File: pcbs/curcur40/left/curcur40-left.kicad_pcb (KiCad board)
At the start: 2 copper layers, 124.3 x 91.8 mm, 79 parts, among them J1 TYPE-C-31-M-13C, J2 TRS, J4 Conn_01x03, SW1 SW_Push, SW10 SW_Push, SW11 SW_Push, SW12 SW_Push, SW13 SW_Push, SW14 SW_Push, SW15 SW_Push, SW16 SW_Push, SW17 SW_Push, SW18 SW_Push, SW2 SW_Push, SW3 SW_Push, SW4 SW_Push, SW5 SW_Push, SW6 SW_Push, SW7 SW_Push, SW8 SW_Push, SW9 SW_Push, U1 RP2040, U2 NCP1117LPST33T3G, U3 TPD4E05U06DQAR, U4 W25Q128JVSIQ, Y1 12MHz 18pF

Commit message: fix
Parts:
- U4: footprint Package_SO:SOIC-8_5.23x5.23mm_P1.27mm -> Package_SO:SOIC-8_5.3x5.3mm_P1.27mm
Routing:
- net Net-(D1-K): track 558.8 -> 552.0 mm, vias 34 -> 32
- net +5V: track 134.4 -> 129.8 mm
- net GND: track 208.4 -> 206.3 mm
- net Net-(EXLED1-DIN): track 135.9 -> 135.1 mm, vias 5 -> 4
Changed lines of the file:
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@@
 		)
 	)
-	(footprint "Package_SO:SOIC-8_5.23x5.23mm_P1.27mm"
+	(footprint "Package_SO:SOIC-8_5.3x5.3mm_P1.27mm"
 		(layer "B.Cu")
 		(at -62.4925 34.64)
@@
 	)
 	(segment
-		(start -29.11475 25.96025)
-		(end -30.5375 24.5375)
-		(width 0.508)
-		(layer "B.Cu")
-		(net "GND")
-	)
-	(segment
 		(start -30.2375 48.65)
 		(end -30.2375 58.2875)
@@
 	)
 	(segment
-		(start -6.5425 38.62)
+		(start -8.5 38.62)
 		(end -24.762 38.62)
 		(width 0.4)
@@
 	)
 	(segment
-		(start -39.235992 41.23995)
-		(end -39.9125 41.23995)
-		(width 0.2032)
-		(layer "F.Cu")
-		(net "+5V")
-	)
-	(segment
 		(start -39.240942 41.235)
 		(end -46.24245 41.235)
@@
 	(segment
 		(start -24.832 30.596)
-		(end -6.5425 30.596)
+		(end -8.5 30.596)
 		(width 0.4)
 		(layer "F.Cu")
@@
 	(segment
 		(start -8.5 38.62)
-		(end -6.5425 38.62)
+		(end -6.5425 38.54625)
 		(width 0.4)
 		(layer "B.Cu")
@@
 	(segment
 		(start -8.5 30.596)
-		(end -6.5425 30.596)
+		(end -6.5425 30.74625)
 		(width 0.4)
 		(layer "B.Cu")
@@
 	)
 	(segment
-		(start -114.5425 4.968751)
-		(end -112.852498 4.968751)
-		(width 0.508)
-		(layer "F.Cu")
-		(net "Net-(D1-K)")
-	)
-	(segment
 		(start -74.2375 -1.663748)
 		(end -73.732498 -2.16875)
@@
 	)
 	(segment
-		(start -112.8325 23.79125)
-		(end -114.9725 23.79125)
-		(width 0.508)
-		(layer "F.Cu")
-		(net "Net-(D1-K)")
-	)
-	(segment
 		(start -112.3275 -13.38505)
 		(end -112.3275 -13.63375)
@@
 	)
 	(segment
-		(start -117.8625 -14.36875)
-		(end -116.4114 -14.36875)
-		(width 0.508)
-		(layer "F.Cu")
-		(net "Net-(D1-K)")
-	)
-	(segment
 		(start -50.15 46.462)
 		(end -50.65 45.4)
@@
 	)
 	(via
-		(at -114.5425 4.968751)
-		(size 0.6)
-		(drill 0.4)
-		(layers "F.Cu" "B.Cu")
-		(capping no)
-		(covering
-			(front no)
-			(back no)
-		)
-		(plugging
-			(front no)
-			(back no)
-		)
-		(filling no)
-		(net "Net-(D1-K)")
-	)
-	(via
 		(at -74.70125 18.375)
 		(size 0.6)
@@
 	)
 	(via
-		(at -114.9725 23.79125)
-		(size 0.6)
-		(drill 0.4)
-		(layers "F.Cu" "B.Cu")
-		(capping no)
-		(covering
-			(front no)
-			(back no)
-		)
-		(plugging
-			(front no)
-			(back no)
-		)
-		(filling no)
-		(net "Net-(D1-K)")
-	)
-	(via
 		(at -23.5 40.135)
 		(size 0.5)
@@
 	)
 	(segment
-		(start -115.6225 24.44125)
-		(end -114.9725 23.79125)
-		(width 0.508)
-		(layer "B.Cu")
-		(net "Net-(D1-K)")
-	)
-	(segment
 		(start -17.08 13.6125)
 		(end -17.0725 13.605)
@@
 	)
 	(segment
-		(start -114.5425 4.968751)
-		(end -115.014999 5.44125)
-		(width 0.508)
-		(layer "B.Cu")
-		(net "Net-(D1-K)")
-	)
-	(segment
 		(start -25.402502 -4.5825)
 		(end -26.4625 -5.642498)
@@
 	)
 	(segment
-		(start -112.9191 -11.76285)
-		(end -112.3375 -11.18125)
-		(width 0.2032)
-		(layer "F.Cu")
-		(net "Net-(EXLED1-DIN)")
-	)
-	(segment
 		(start -20.0225 -4.6915)
 		(end -18.04025 -4.6915)
@@
 		(size 0.6)
 		(drill 0.4)
-		(layers "F.Cu" "B.Cu")
-		(capping no)
-		(covering
-			(front no)
-			(back no)
-		)
-		(plugging
-			(front no)
-			(back no)
-		)
-		(filling no)
-		(net "Net-(EXLED1-DIN)")
-	)
-	(via
-		(at -112.3375 -11.18125)
-		(size 0.6)
-		(drill 0.4)

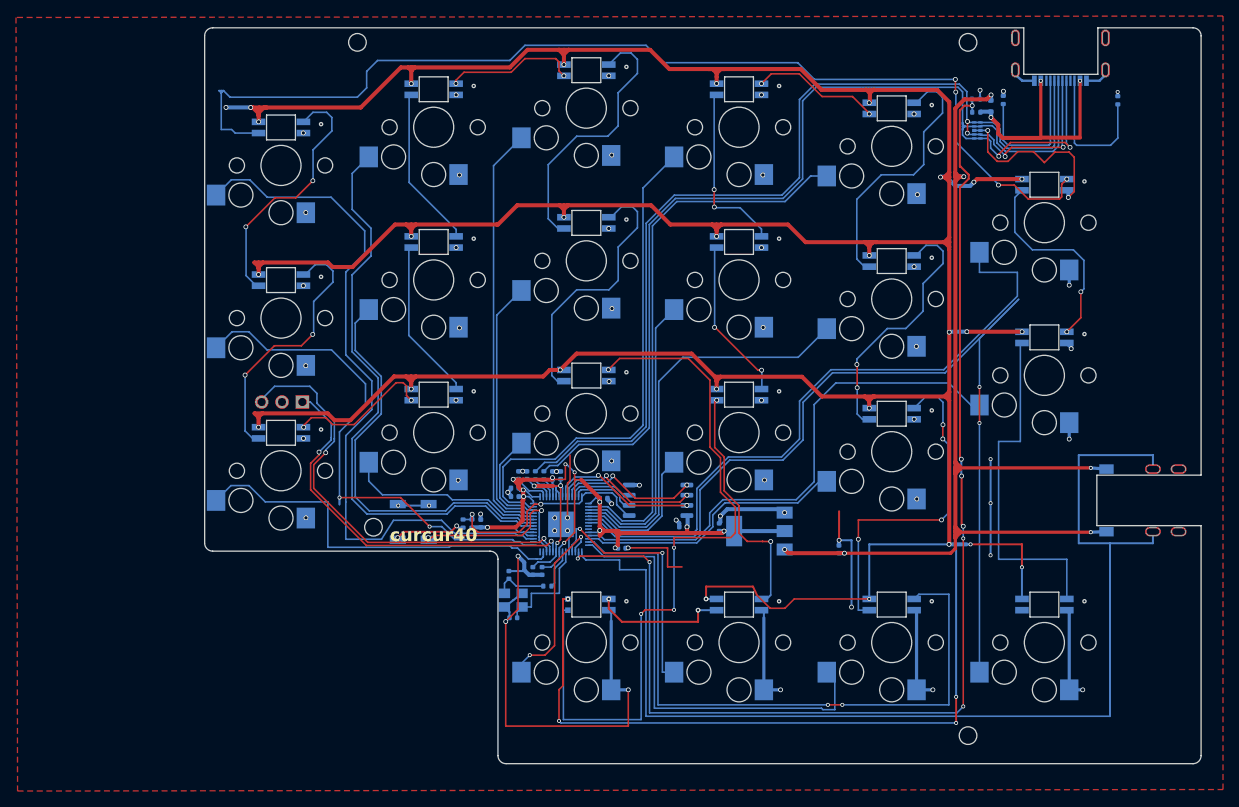
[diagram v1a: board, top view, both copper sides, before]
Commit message: 🔴 1. 致命的な不具合（Critical：物理的に組立不可、または動作不可）
[Critical-1] トラックボール部の3D機構・光学設計の破綻（4重の物理的干渉・焦点外れ）
[Critical-2] 左右メイン基板の取付穴径が ∅2.20 mm になっており、M2スペーサーが貫通できない
[Critical-3] 3Dプリントケース内部の 2.0mm スペーサー受けボスが消失しており、高さが 2.0 mm 合わない
[Critical-4] PMW3360 センサー基板のプルアップ抵抗 R1（10kΩ）が PCBA の BOM/CPL から除外されており、リセット端子（NRESET）がフローティング（不定）になる
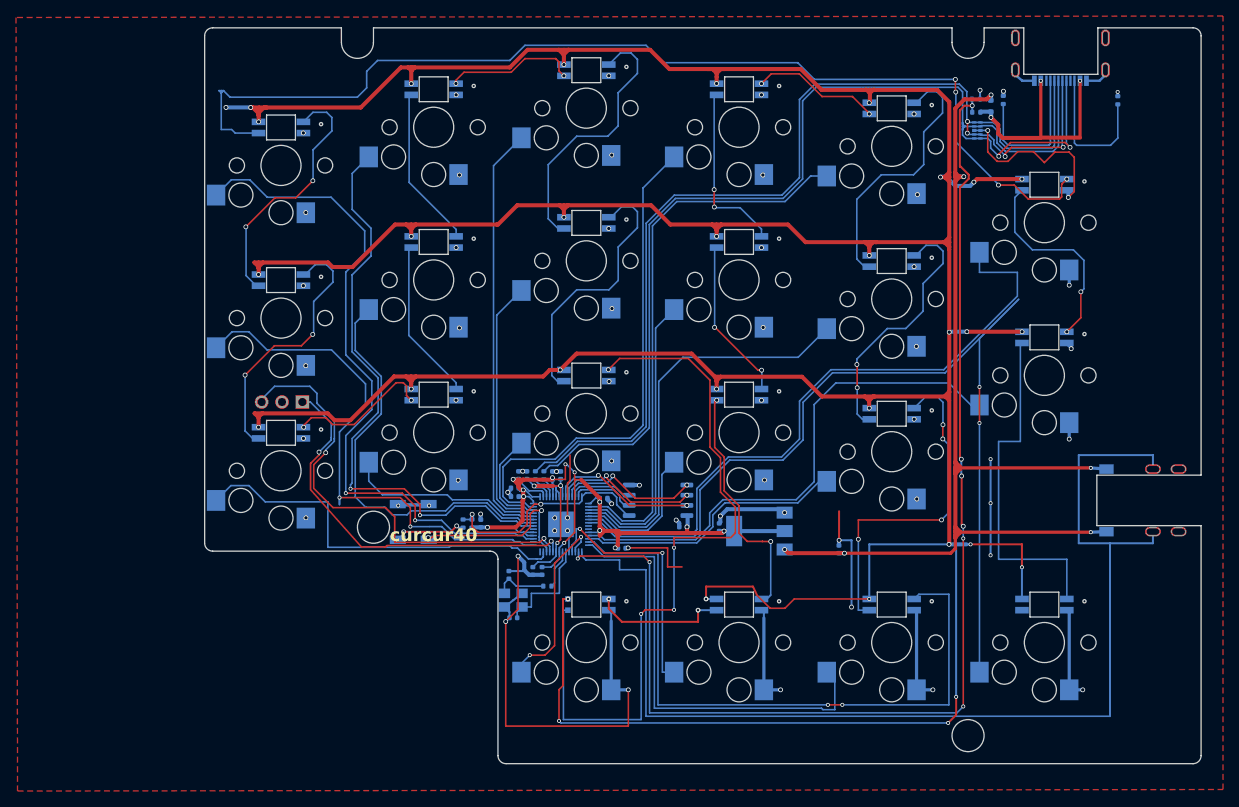
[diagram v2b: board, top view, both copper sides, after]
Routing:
- net /KEY18: track 89.8 -> 85.2 mm, vias 0 -> 2
- net GND: track 206.3 -> 210.2 mm
- net /SWD: track 55.8 -> 57.7 mm
- net /KEY17: track 66.1 -> 67.5 mm
- net Net-(D1-K): track 552.0 -> 551.4 mm
- net /KEY13: track 73.0 -> 73.5 mm, vias 0 -> 2
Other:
- outline, holes or cut-outs redrawn

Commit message: fix hole
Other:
- outline, holes or cut-outs redrawn
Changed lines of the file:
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@@
 	(gr_line
 		(start -118.0625 -24.3125)
-		(end -102 -24.3125)
+		(end -16.8575 -24.3125)
 		(stroke
 			(width 0.1)
@@
 		(layer "Edge.Cuts")
 	)
-	(gr_line
-		(start -102 -24.3125)
-		(end -102 -22.5)
+	(gr_circle
+		(center -109.5375 -20)
+		(end -107.7375 -20)
 		(stroke
 			(width 0.1)
 			(type default)
 		)
-		(layer "Edge.Cuts")
-	)
-	(gr_line
-		(start -98 -24.3125)
-		(end -25.8125 -24.3125)
-		(stroke
-			(width 0.1)
-			(type default)
-		)
-		(layer "Edge.Cuts")
-	)
-	(gr_arc
-		(start -98 -22.5)
-		(mid -100 -20.5)
-		(end -102 -22.5)
-		(stroke
-			(width 0.1)
-			(type default)
-		)
-		(layer "Edge.Cuts")
-	)
-	(gr_line
-		(start -98 -22.5)
-		(end -98 -24.3125)
-		(stroke
-			(width 0.1)
-			(type default)
-		)
+		(fill no)
 		(layer "Edge.Cuts")
 	)
 	(gr_circle
 		(center -98 38)
-		(end -96 38)
+		(end -96.2 38)
 		(stroke
 			(width 0.1)
@@
 		(layer "Edge.Cuts")
 	)
-	(gr_line
-		(start -25.8125 -24.3125)
-		(end -25.8125 -22.5)
-		(stroke
-			(width 0.1)
-			(type default)
-		)
-		(layer "Edge.Cuts")
-	)
 	(gr_circle
 		(center -23.8125 64)
-		(end -21.8125 64)
+		(end -22.0125 64)
 		(stroke
 			(width 0.1)
@@
 		)
 		(fill no)
-		(layer "Edge.Cuts")
-	)
-	(gr_line
-		(start -21.8125 -24.3125)
-		(end -16.8575 -24.3125)
-		(stroke
-			(width 0.1)
-			(type default)
-		)
-		(layer "Edge.Cuts")
-	)
-	(gr_arc
-		(start -21.8125 -22.5)
-		(mid -23.8125 -20.5)
-		(end -25.8125 -22.5)
-		(stroke
-			(width 0.1)
-			(type default)
-		)
-		(layer "Edge.Cuts")
-	)
-	(gr_line
-		(start -21.8125 -22.5)
-		(end -21.8125 -24.3125)
-		(stroke
-			(width 0.1)
-			(type default)
-		)
 		(layer "Edge.Cuts")
 	)
@@
 		(layer "Edge.Cuts")
 	)
+	(gr_circle
+		(center 0 -15)
+		(end 1.8 -15)
+		(stroke
+			(width 0.1)
+			(type default)
+		)
+		(fill no)
+		(layer "Edge.Cuts")
+	)
+	(gr_circle
+		(center 0 25)
+		(end 1.8 25)
+		(stroke
+			(width 0.1)
+			(type default)
+		)
+		(fill no)
+		(layer "Edge.Cuts")
+	)

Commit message: シルク文字
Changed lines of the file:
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@@
 	)
 	(gr_text "curcur40"
-		(at -90.4875 38.98125 0)
+		(at -52.3875 64 0)
 		(layer "F.SilkS")
 		(effects

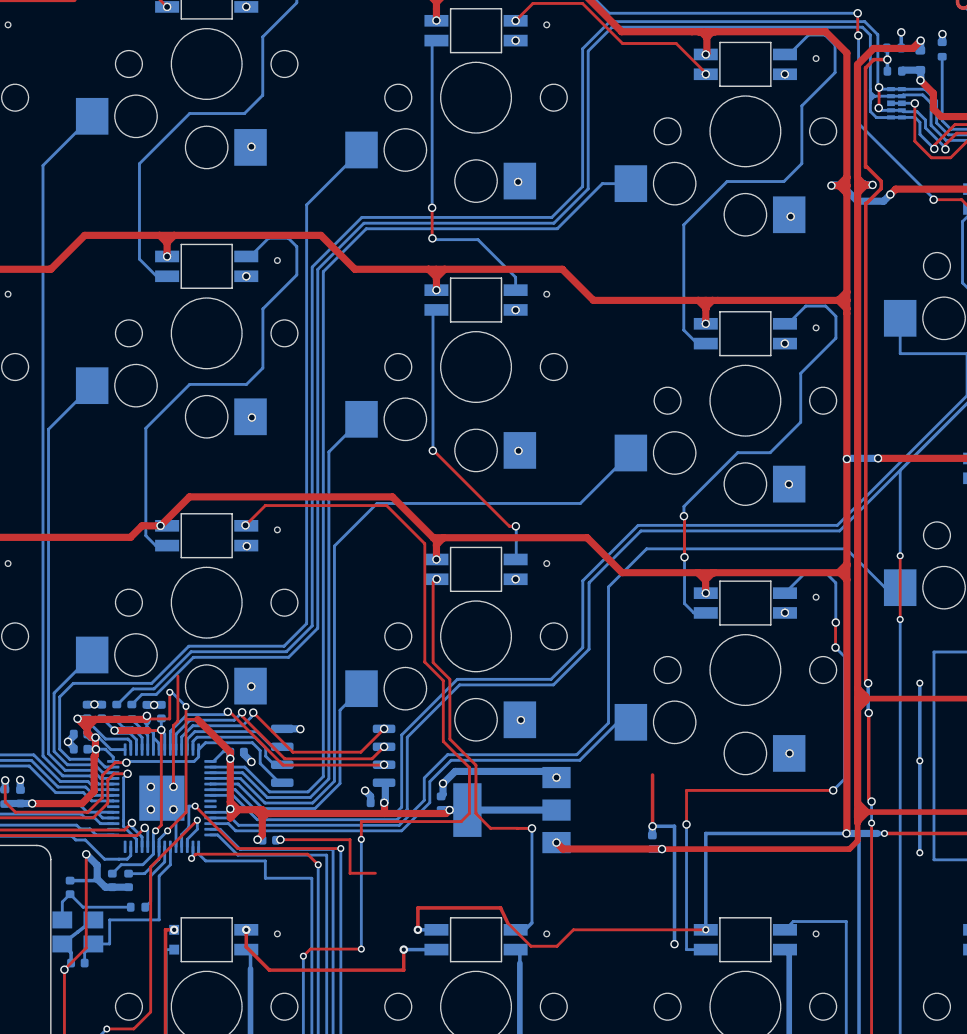
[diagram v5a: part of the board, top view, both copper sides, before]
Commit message: fix(pcb): eliminate all ERC/DRC/parity warnings and ignored DRC checks on left and right PCBs
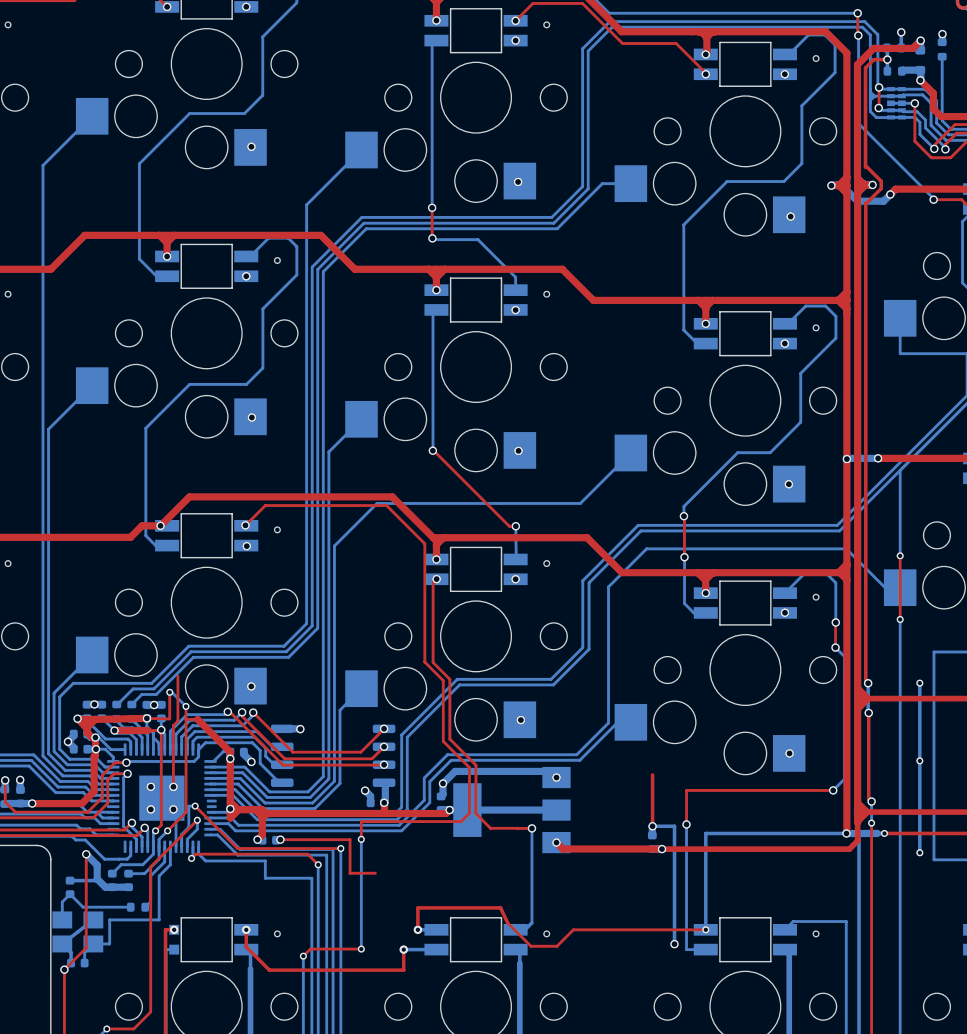
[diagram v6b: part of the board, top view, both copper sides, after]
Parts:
- LED9: footprint kbd_local:YS-SK6812MINI-E -> kbd_local:YS-SK6812MINI-E_LED9
- SW1: footprint kbd_local:keyswitch_choc12_hotswap_1u -> kbd_local:keyswitch_choc12_hotswap_1.5u
- Y1: footprint Crystal:Crystal_SMD_3225-4Pin_3.2x2.5mm -> Crystal:Crystal_SMD_3225-4Pin_3.2x2.5mm_Left

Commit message: Refactor PCBs and schematics to use genuine KiCad 10.0 standard libraries and isolate PMW3360 VDDPIX
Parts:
- EXLED1, EXLED2, EXLED3, LED1, LED10, LED11, LED12, LED13, LED14, LED15, LED16, LED17, LED18, LED2, LED3, LED4, LED5, LED6, LED7, LED8: footprint kbd_local:YS-SK6812MINI-E -> kbd:YS-SK6812MINI-E
- EXSW1, EXSW2, EXSW3, SW10, SW11, SW12, SW13, SW14, SW15, SW16, SW17, SW18, SW2, SW3, SW4, SW5, SW6, SW7, SW8, SW9: footprint kbd_local:keyswitch_choc12_hotswap_1u -> kbd:keyswitch_choc12_hotswap_1u
- J1: footprint kbd_local:TYPE-C-31-M-13C -> kbd:USB_C_Receptacle_TYPE-C-31-M-13C
- J2: footprint kbd_local:PJ-398A-5A_PJ-399B-6A -> kbd:Jack_PJ-398A-5A_PJ-399B-6A
- LED9: footprint kbd_local:YS-SK6812MINI-E_LED9 -> kbd:YS-SK6812MINI-E_LED9
- SMDSW1, SMDSW2: footprint kbd_local:TS-1088R-02026 -> kbd:TS-1088R-02026
- SW1: footprint kbd_local:keyswitch_choc12_hotswap_1.5u -> kbd:keyswitch_choc12_hotswap_1.5u
- Y1: footprint Crystal:Crystal_SMD_3225-4Pin_3.2x2.5mm_Left -> Crystal:Crystal_SMD_3225-4Pin_3.2x2.5mm
- moved Y1 0.35 mm to (-80.2, 47.1)
- moved C16 0.06 mm to (-59.4, 38.0)
- moved C1 0.05 mm to (-80.5, 49.4)

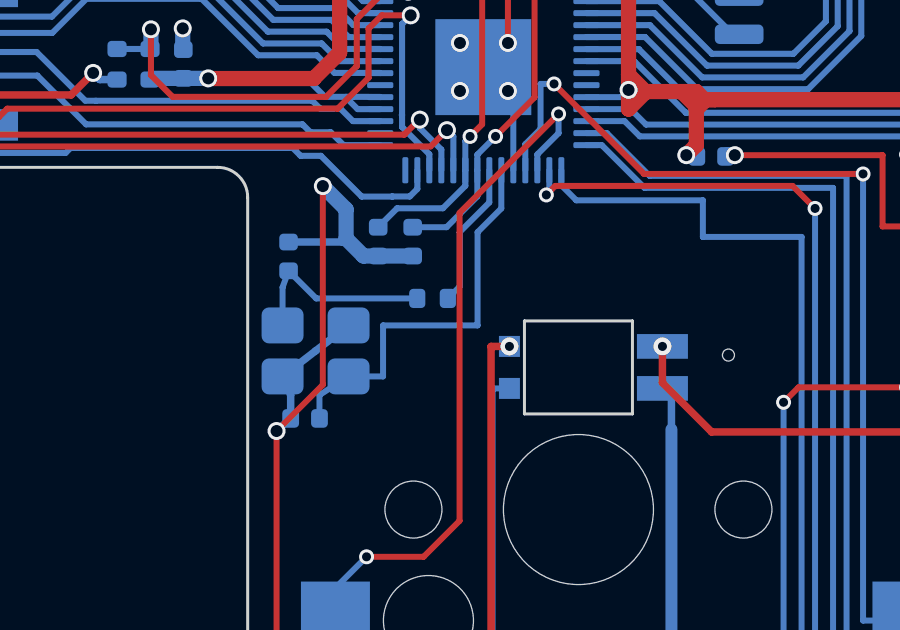
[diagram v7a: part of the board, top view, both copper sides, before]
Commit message: Clean up unused custom library files, fix fp-lib-table, and mark SWD headers J4/rJ4 as DNP
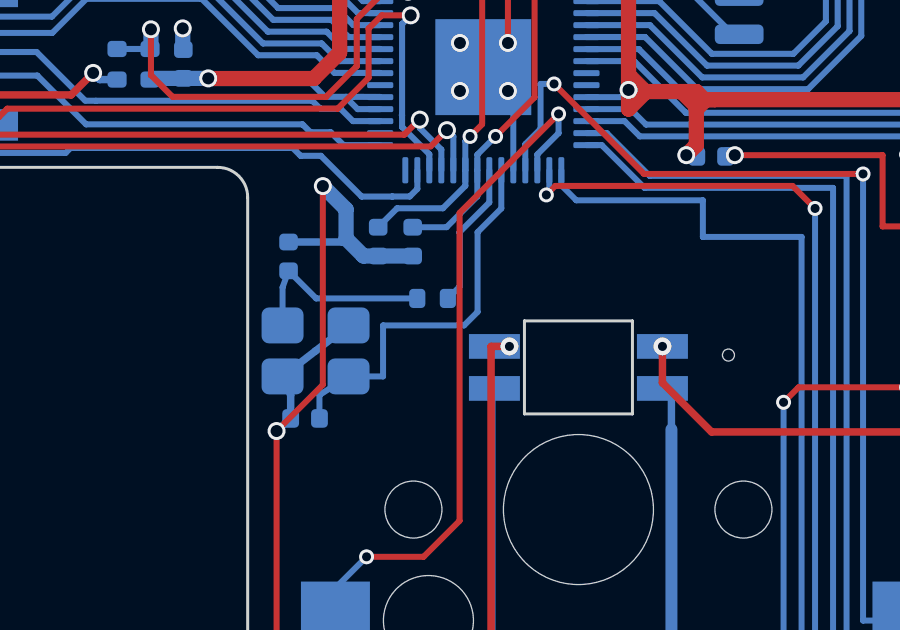
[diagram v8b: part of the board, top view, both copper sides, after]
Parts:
- LED9: footprint kbd:YS-SK6812MINI-E_LED9 -> kbd:YS-SK6812MINI-E
